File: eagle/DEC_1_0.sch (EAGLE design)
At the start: 14 parts, among them IC1 74HC138N, X1 In, X2 Ctrl, X3 Out A, X4 Out B

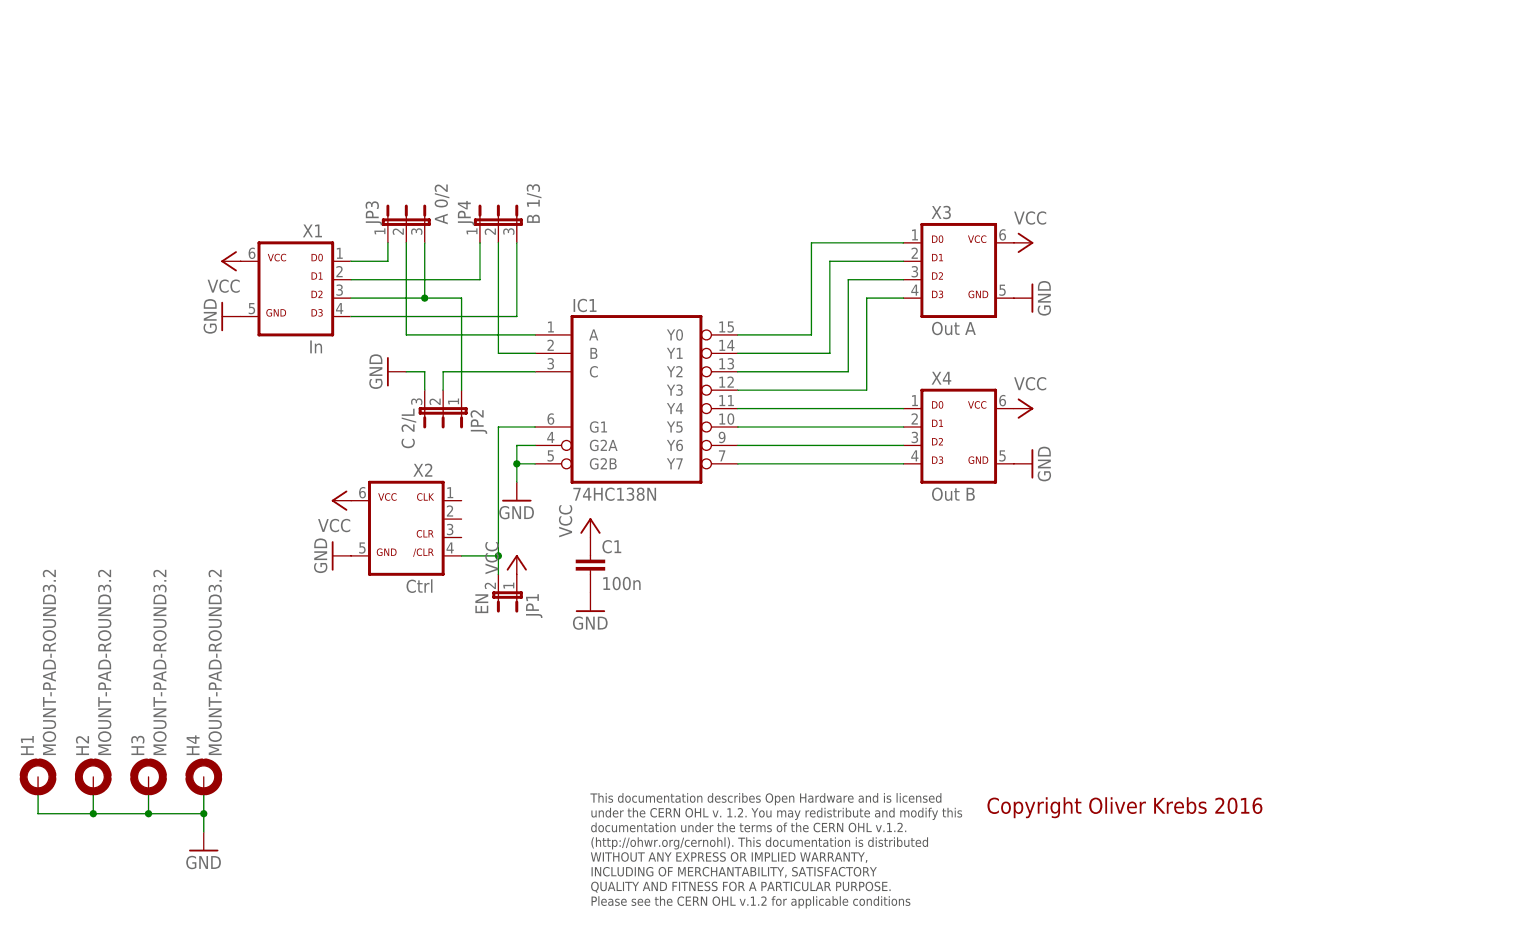
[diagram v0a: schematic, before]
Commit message: Add new tetra-Board and arduino files
Add AMP_1_0, AVC_1_0, D18_1_1, IOP_1_2, MIC_1_0, PIN_1_1, POT_1_0, PWA_1_0, PWR_1_0, RGF 2.0, SOC_2_0, VLT_1_0
Add mex_nano_shield_keyboard, mex_nano_shied_numbers

New arduino projects
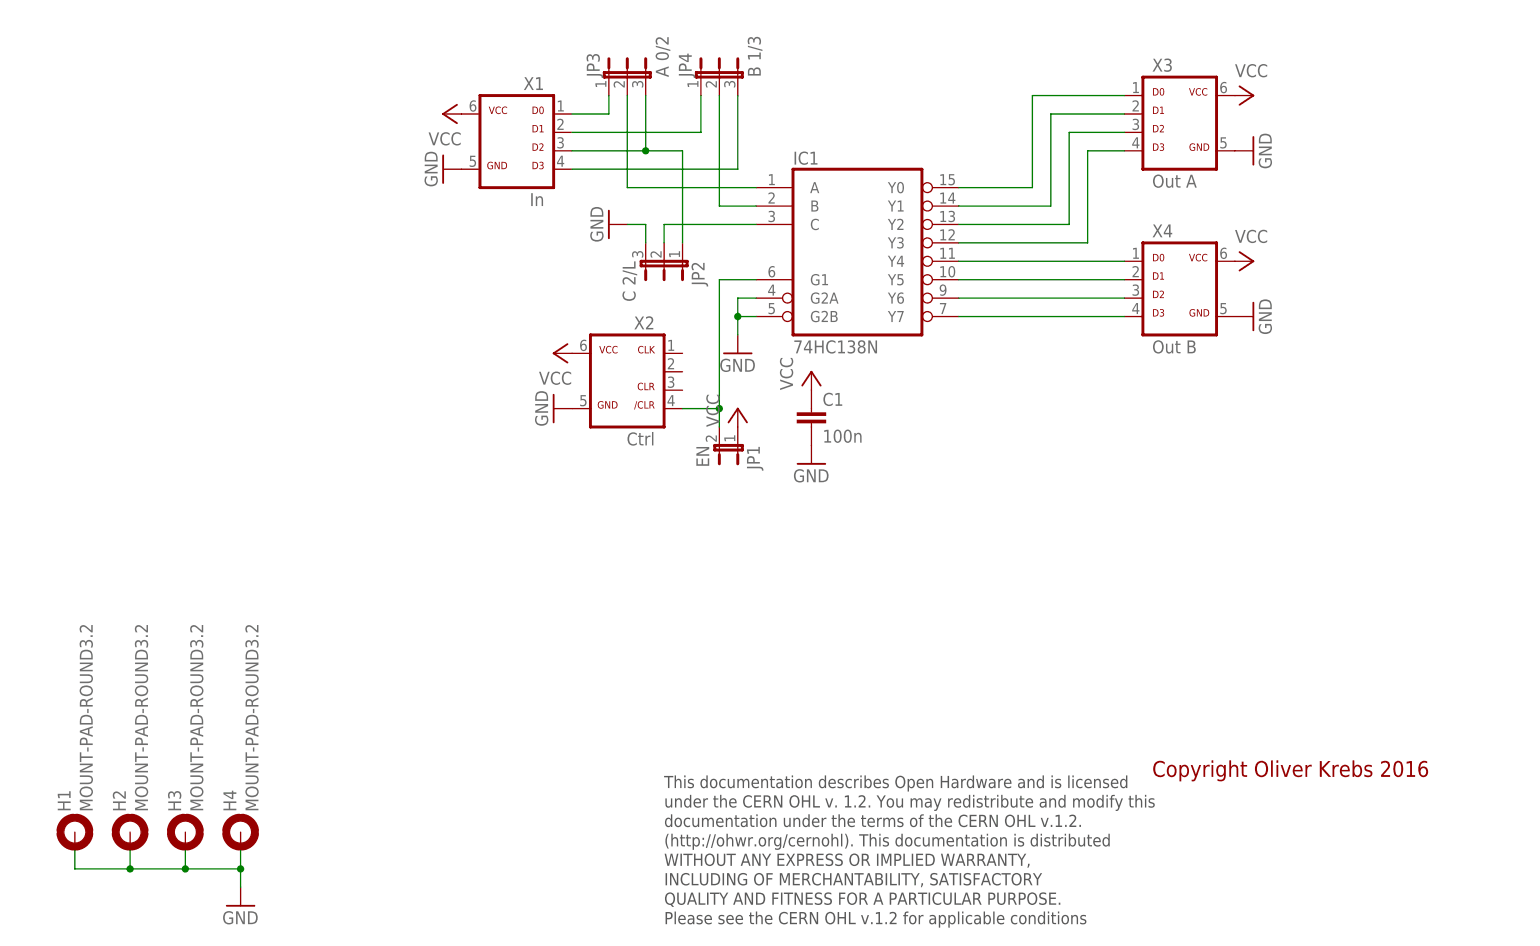
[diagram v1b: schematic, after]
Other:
- moved on the sheet: C1, H1, H2, H3, H4, IC1, JP1, JP2, JP3, JP4, X1, X2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
